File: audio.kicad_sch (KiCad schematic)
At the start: 5 parts, among them J3 Conn_01x02, U3 MAX98357A

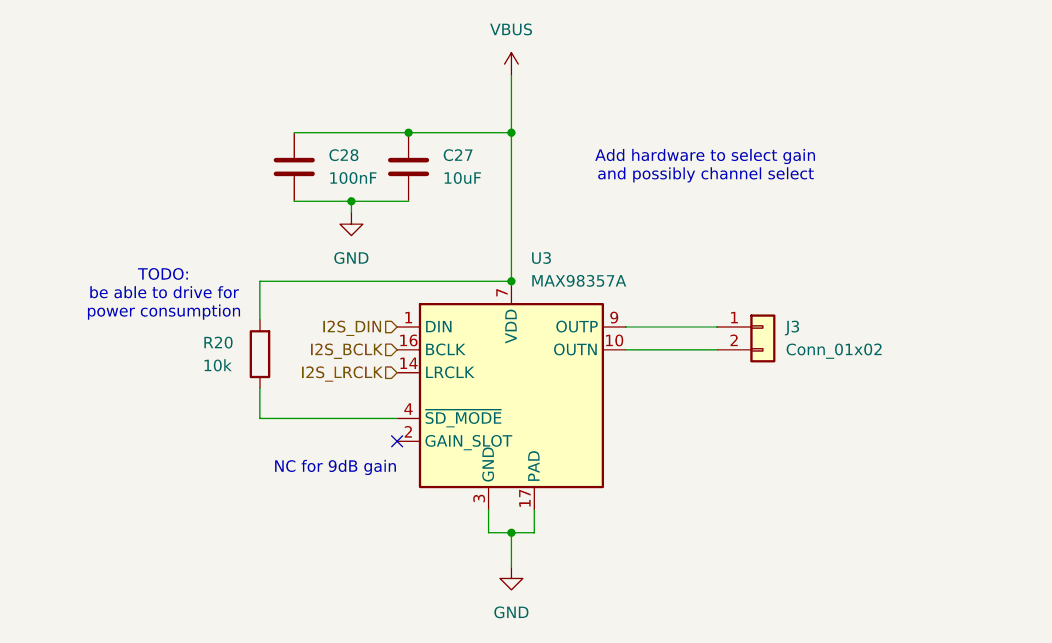
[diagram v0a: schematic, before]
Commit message: add amplifier mode selector, add drawing lcd
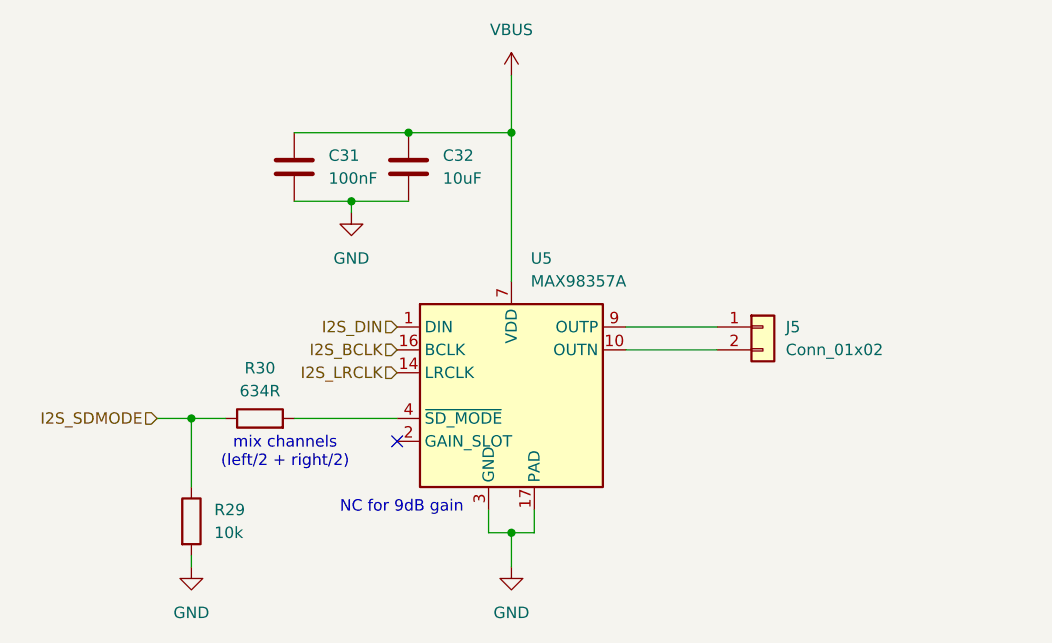
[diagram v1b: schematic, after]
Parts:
- removed R20: 10k, Resistor_SMD:R_0603_1608Metric, symbol Device:R
- added R29: 10k, symbol Device:R
- added R30: 634R, symbol Device:R
- renumbered C28 to C31, C27 to C32, J3 to J5, U3 to U5
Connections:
- net GND: now also R29.2
- net at U5.4 (~{SD_MODE}): now also R30.2
- new net I2S_SDMODE: R29.1, R30.1
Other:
- note added: "mix channels (left/2 + right/2)"
- note removed: "Add hardware to select gain and possibly channel select"
- note removed: "TODO: be able to drive for power consumption"

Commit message: add on/off switch
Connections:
- net VBUS renamed +5V

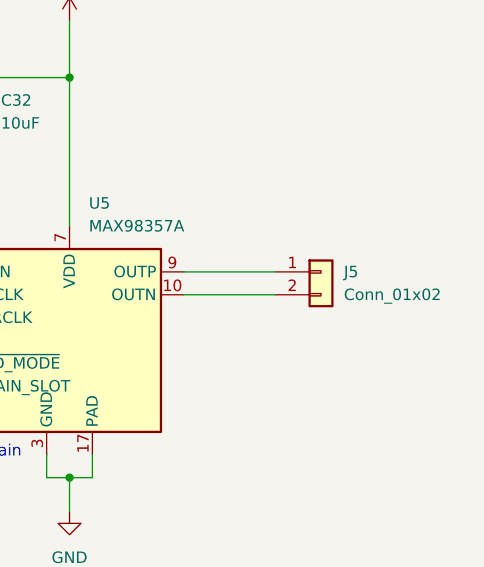
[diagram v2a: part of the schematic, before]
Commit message: add SD card
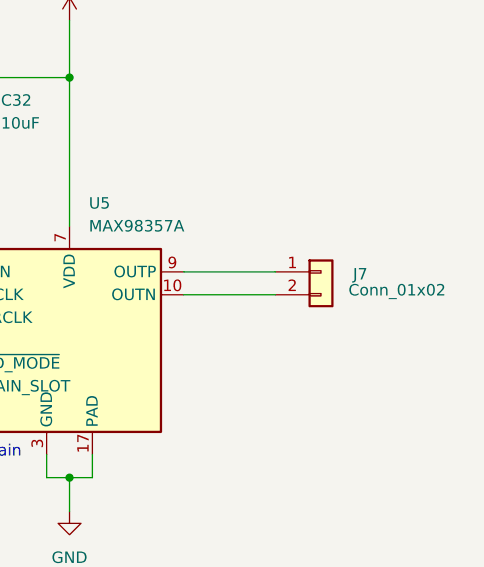
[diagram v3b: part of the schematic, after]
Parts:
- removed J5: Conn_01x02, symbol Connector_Generic:Conn_01x02
- added J7: Conn_01x02, Connector_JST:JST_PH_B2B-PH-K_1x02_P2.00mm_Vertical, symbol Connector_Generic:Conn_01x02
- C31: footprint (none) -> Capacitor_SMD:C_0603_1608Metric
- C32: footprint (none) -> Capacitor_SMD:C_0805_2012Metric
- R29, R30: footprint (none) -> Resistor_SMD:R_0603_1608Metric
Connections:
- net at U5.9 (OUTP): now also J7.1 (Pin_1)
- net at U5.10 (OUTN): now also J7.2 (Pin_2)
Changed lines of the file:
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@@
 			)
 		)
-		(property "Footprint" ""
+		(property "Footprint" "Resistor_SMD:R_0603_1608Metric"
 			(at 96.012 113.03 90)
 			(effects
@@
 	)
 	(symbol
-		(lib_id "Connector_Generic:Conn_01x02")
-		(at 161.29 91.44 0)
-		(unit 1)
-		(exclude_from_sim no)
-		(in_bom yes)
-		(on_board yes)
-		(dnp no)
-		(fields_autoplaced yes)
-		(property "Reference" "J5"
-			(at 163.83 91.4399 0)
-			(effects
-				(font
-					(size 1.27 1.27)
-				)
-				(justify left)
-			)
-		)
-		(property "Value" "Conn_01x02"
-			(at 163.83 93.9799 0)
-			(effects
-				(font
-					(size 1.27 1.27)
-				)
-				(justify left)
-			)
-		)
-		(property "Footprint" ""
-			(at 161.29 91.44 0)
-			(effects
-				(font
-					(size 1.27 1.27)
-				)
-				(hide yes)
-			)
-		)
-		(property "Datasheet" "~"
-			(at 161.29 91.44 0)
-			(effects
-				(font
-					(size 1.27 1.27)
-				)
-				(hide yes)
-			)
-		)
-		(property "Description" "Generic connector, single row, 01x02, script generated (kicad-library-utils/schlib/autogen/connector/)"
-			(at 161.29 91.44 0)
-			(effects
-				(font
-					(size 1.27 1.27)
-				)
-				(hide yes)
-			)
-		)
-		(pin "1"
-		)
-		(pin "2"
-		)
-		(instances
-			(project ""
-				(path "/f4643692-c319-40a7-82a2-3e775c0a417f/544a4a01-8cf8-45b3-bce5-8d02a4ea8581"
-					(reference "J5")
-					(unit 1)
-				)
-			)
-		)
-	)
-	(symbol
 		(lib_id "Device:R")
 		(at 105.41 101.6 90)
@@
 			)
 		)
-		(property "Footprint" ""
+		(property "Footprint" "Resistor_SMD:R_0603_1608Metric"
 			(at 105.41 103.378 90)
 			(effects
@@
 			)
 		)
-		(property "Footprint" ""
+		(property "Footprint" "Capacitor_SMD:C_0805_2012Metric"
 			(at 122.8852 77.47 0)
 			(effects
@@
 	)
 	(symbol
+		(lib_id "Connector_Generic:Conn_01x02")
+		(at 161.29 91.44 0)
+		(unit 1)
+		(exclude_from_sim no)
+		(in_bom yes)
+		(on_board yes)
+		(dnp no)
+		(property "Reference" "J7"
+			(at 164.846 91.694 0)
+			(effects
+				(font
+					(size 1.27 1.27)
+				)
+				(justify left)
+			)
+		)
+		(property "Value" "Conn_01x02"
+			(at 164.338 93.472 0)
+			(effects
+				(font
+					(size 1.27 1.27)
+				)
+				(justify left)
+			)
+		)
+		(property "Footprint" "Connector_JST:JST_PH_B2B-PH-K_1x02_P2.00mm_Vertical"
+			(at 161.29 91.44 0)
+			(effects
+				(font
+					(size 1.27 1.27)
+				)
+				(hide yes)
+			)
+		)
+		(property "Datasheet" "~"
+			(at 161.29 91.44 0)
+			(effects
+				(font
+					(size 1.27 1.27)
+				)
+				(hide yes)
+			)
+		)
+		(property "Description" "Generic connector, single row, 01x02, script generated (kicad-library-utils/schlib/autogen/connector/)"
+			(at 161.29 91.44 0)
+			(effects
+				(font
+					(size 1.27 1.27)
+				)
+				(hide yes)
+			)
+		)
+		(property "LCSC" "C131337"
+			(at 161.29 91.44 0)
+			(effects
+				(font
+					(size 1.27 1.27)
+				)
+				(hide yes)
+			)
+		)
+		(property "Manufacturer" "JST"
+			(at 161.29 91.44 0)
+			(effects
+				(font
+					(size 1.27 1.27)
+				)
+				(hide yes)
+			)
+		)
+		(property "Manufacturer Part Number" "B2B-PH-K-S(LF)(SN)"
+			(at 161.29 91.44 0)
+			(effects
+				(font
+					(size 1.27 1.27)
+				)
+				(hide yes)
+			)
+		)
+		(pin "2"
+		)
+		(pin "1"
+		)
+		(instances
+			(project "gameboy"
+				(path "/f4643692-c319-40a7-82a2-3e775c0a417f/544a4a01-8cf8-45b3-bce5-8d02a4ea8581"
+					(reference "J7")
+					(unit 1)
+				)
+			)
+		)
+	)
+	(symbol
 		(lib_id "power:+5V")
 		(at 133.35 63.5 0)
@@
 			)
 		)
-		(property "Footprint" ""
+		(property "Footprint" "Capacitor_SMD:C_0603_1608Metric"
 			(at 110.1852 77.47 0)
 			(effects

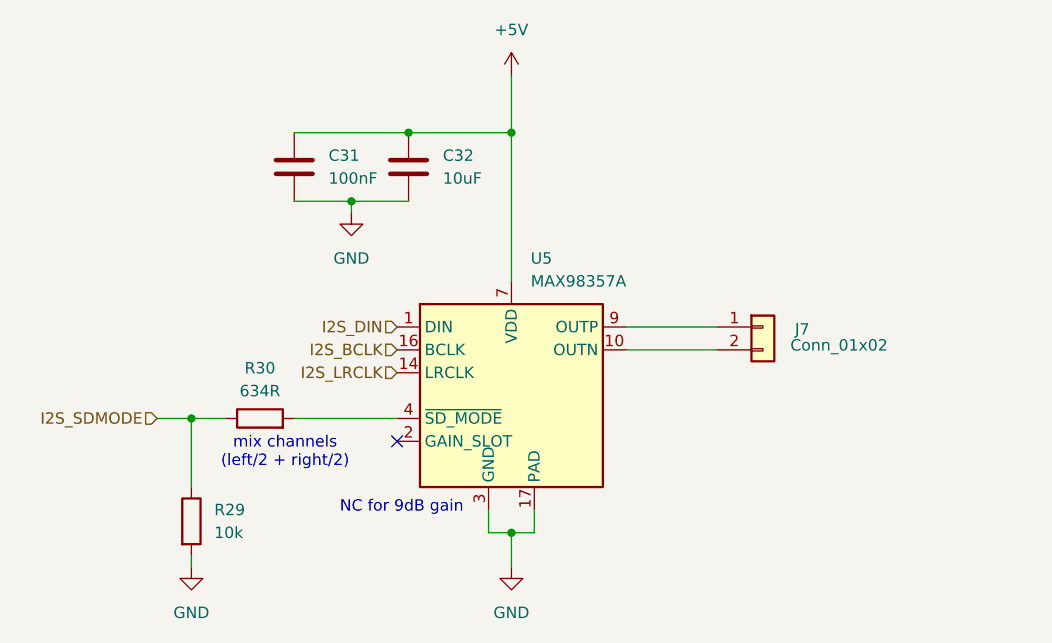
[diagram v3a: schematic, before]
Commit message: fix usb and add esd diodes, some other checks
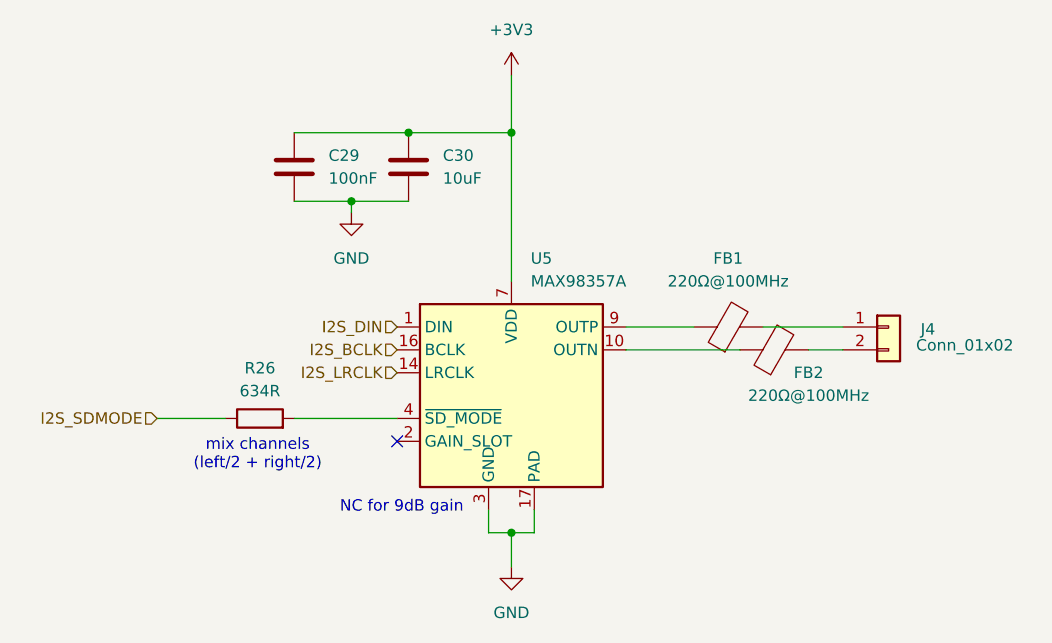
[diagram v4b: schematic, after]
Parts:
- removed R29: 10k, Resistor_SMD:R_0603_1608Metric, symbol Device:R
- added FB1, FB2: 220Ω@100MHz, Inductor_SMD:L_0603_1608Metric, symbol Device:FerriteBead
- renumbered C31 to C29, C32 to C30, J7 to J4, R30 to R26
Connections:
- net at U5.10 (OUTN): now also FB2.1; no longer J4.2 (Pin_2)
- net at U5.9 (OUTP): now also FB1.1; no longer J4.1 (Pin_1)
- net +5V renamed +3V3
- new net: FB1.2, J4.1 (Pin_1)
- new net: FB2.2, J4.2 (Pin_2)
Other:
- moved on the sheet: J4

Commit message: more routing
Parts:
- J4: footprint Connector_JST:JST_PH_B2B-PH-K_1x02_P2.00mm_Vertical -> Connector_JST:JST_PH_S2B-PH-SM4-TB_1x02-1MP_P2.00mm_Horizontal; LCSC C131337 -> C295747; Manufacturer Part Number B2B-PH-K-S(LF)(SN) -> S2B-PH-SM4-TB(LF)(SN)
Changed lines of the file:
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@@
+	)
+	(symbol
+		(lib_id "Connector_Generic:Conn_01x02")
+		(at 175.26 91.44 0)
+		(unit 1)
+		(exclude_from_sim no)
+		(in_bom yes)
+		(on_board yes)
+		(dnp no)
+		(property "Reference" "J4"
+			(at 178.816 91.694 0)
+			(effects
+				(font
+					(size 1.27 1.27)
+				)
+				(justify left)
+			)
+		)
+		(property "Value" "Conn_01x02"
+			(at 178.308 93.472 0)
+			(effects
+				(font
+					(size 1.27 1.27)
+				)
+				(justify left)
+			)
+		)
+		(property "Footprint" "Connector_JST:JST_PH_S2B-PH-SM4-TB_1x02-1MP_P2.00mm_Horizontal"
+			(at 175.26 91.44 0)
+			(effects
+				(font
+					(size 1.27 1.27)
+				)
+				(hide yes)
+			)
+		)
+		(property "Datasheet" "~"
+			(at 175.26 91.44 0)
+			(effects
+				(font
+					(size 1.27 1.27)
+				)
+				(hide yes)
+			)
+		)
+		(property "Description" "Generic connector, single row, 01x02, script generated (kicad-library-utils/schlib/autogen/connector/)"
+			(at 175.26 91.44 0)
+			(effects
+				(font
+					(size 1.27 1.27)
+				)
+				(hide yes)
+			)
+		)
+		(property "LCSC" "C295747"
+			(at 175.26 91.44 0)
+			(effects
+				(font
+					(size 1.27 1.27)
+				)
+				(hide yes)
+			)
+		)
+		(property "Manufacturer" "JST"
+			(at 175.26 91.44 0)
+			(effects
+				(font
+					(size 1.27 1.27)
+				)
+				(hide yes)
+			)
+		)
+		(property "Manufacturer Part Number" "S2B-PH-SM4-TB(LF)(SN)"
+			(at 175.26 91.44 0)
+			(effects
+				(font
+					(size 1.27 1.27)
+				)
+				(hide yes)
+			)
+		)
+		(pin "2"
+		)
+		(pin "1"
+		)
+		(instances
+			(project "gameboy"
+				(path "/f4643692-c319-40a7-82a2-3e775c0a417f/544a4a01-8cf8-45b3-bce5-8d02a4ea8581"
+					(reference "J4")
+					(unit 1)
+				)
+			)
+		)
 	)
 	(symbol
@@
 					(unit 1)
 				)
-			)
-		)
-	)
-	(symbol
-		(lib_id "Connector_Generic:Conn_01x02")
-		(at 175.26 91.44 0)
-		(unit 1)
-		(exclude_from_sim no)
-		(in_bom yes)
-		(on_board yes)
-		(dnp no)
-		(property "Reference" "J4"
-			(at 178.816 91.694 0)
-			(effects
-				(font
-					(size 1.27 1.27)
-				)
-				(justify left)
-			)
-		)
-		(property "Value" "Conn_01x02"
-			(at 178.308 93.472 0)
-			(effects
-				(font
-					(size 1.27 1.27)
-				)
-				(justify left)
-			)
-		)
-		(property "Footprint" "Connector_JST:JST_PH_B2B-PH-K_1x02_P2.00mm_Vertical"
-			(at 175.26 91.44 0)
-			(effects
-				(font
-					(size 1.27 1.27)
-				)
-				(hide yes)
-			)
-		)
-		(property "Datasheet" "~"
-			(at 175.26 91.44 0)
-			(effects
-				(font
-					(size 1.27 1.27)
-				)
-				(hide yes)
-			)
-		)
-		(property "Description" "Generic connector, single row, 01x02, script generated (kicad-library-utils/schlib/autogen/connector/)"
-			(at 175.26 91.44 0)
-			(effects
-				(font
-					(size 1.27 1.27)
-				)
-				(hide yes)
-			)
-		)
-		(property "LCSC" "C131337"
-			(at 175.26 91.44 0)
-			(effects
-				(font
-					(size 1.27 1.27)
-				)
-				(hide yes)
-			)
-		)
-		(property "Manufacturer" "JST"
-			(at 175.26 91.44 0)
-			(effects
-				(font
-					(size 1.27 1.27)
-				)
-				(hide yes)
-			)
-		)
-		(property "Manufacturer Part Number" "B2B-PH-K-S(LF)(SN)"
-			(at 175.26 91.44 0)
-			(effects
-				(font
-					(size 1.27 1.27)
-				)
-				(hide yes)
-			)
-		)
-		(pin "2"
-		)
-		(pin "1"
-		)
-		(instances
-			(project "gameboy"
-				(path "/f4643692-c319-40a7-82a2-3e775c0a417f/544a4a01-8cf8-45b3-bce5-8d02a4ea8581"
-					(reference "J4")
-					(unit 1)
-				)

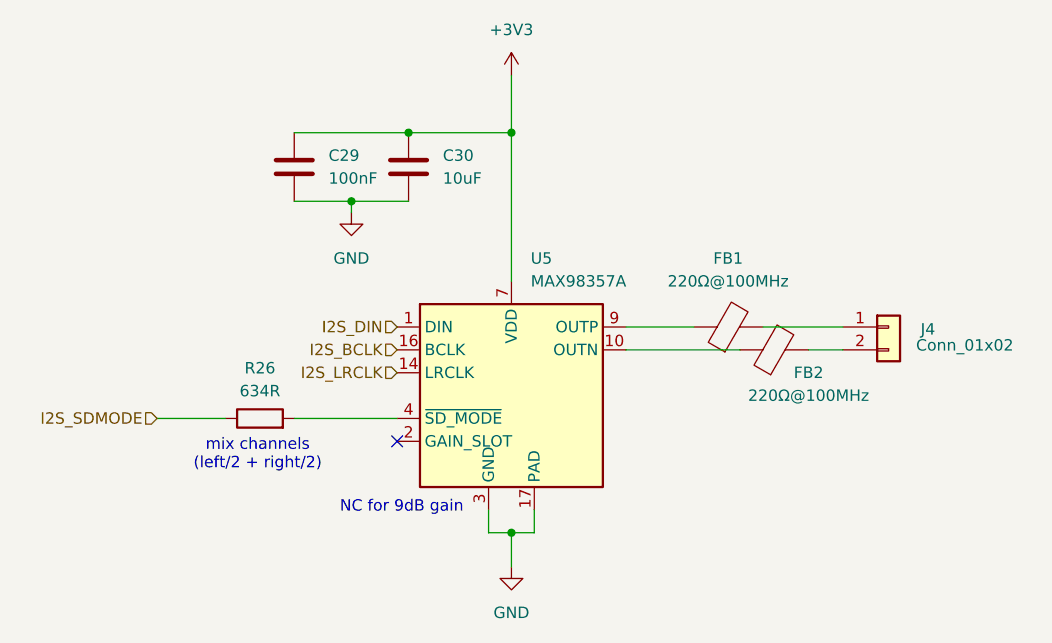
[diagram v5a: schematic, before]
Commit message: add silkscreen, optimize layout and replace sd card peripheral
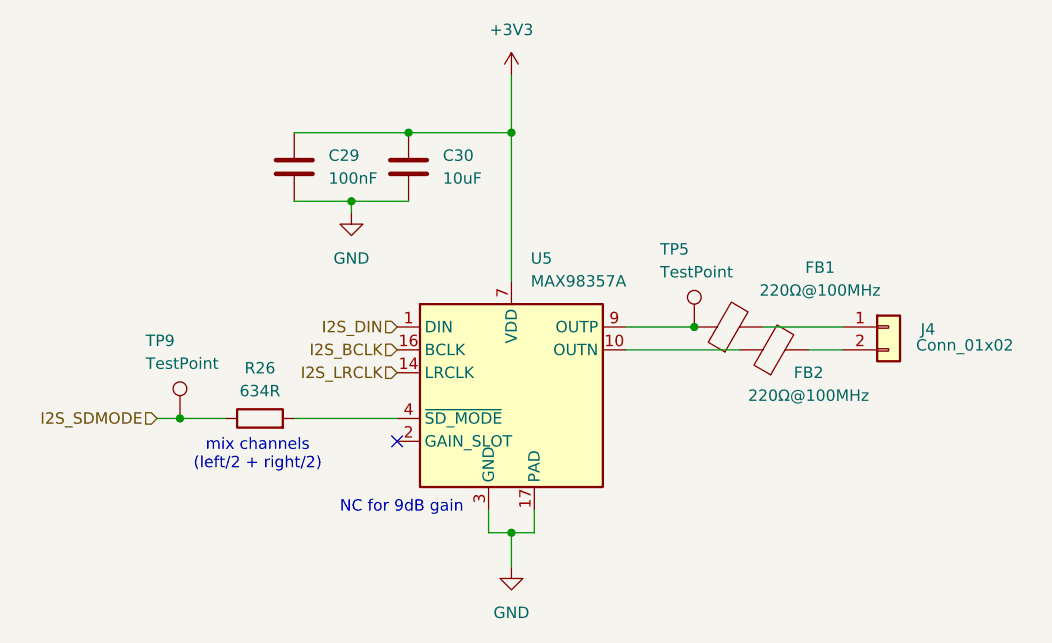
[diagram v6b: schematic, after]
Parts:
- added TP5, TP9: TestPoint, TestPoint:TestPoint_Pad_D1.0mm, symbol Connector:TestPoint
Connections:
- net I2S_SDMODE: now also TP9.1
- net at FB1.1, U5.9 (OUTP): now also TP5.1
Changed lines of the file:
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@@
+	)
+	(junction
+		(at 153.67 91.44)
+		(diameter 0)
+		(color 0 0 0 0)
 	)
 	(junction
@@
 	)
 	(junction
+		(at 96.52 101.6)
+		(diameter 0)
+		(color 0 0 0 0)
+	)
+	(junction
 		(at 121.92 69.85)
 		(diameter 0)
@@
 	(wire
 		(pts
-			(xy 93.98 101.6) (xy 101.6 101.6)
+			(xy 93.98 101.6) (xy 96.52 101.6)
 		)
 		(stroke
@@
 		(pts
 			(xy 161.29 91.44) (xy 170.18 91.44)
+		)
+		(stroke
+			(width 0)
+			(type default)
+		)
+	)
+	(wire
+		(pts
+			(xy 96.52 101.6) (xy 101.6 101.6)
 		)
 		(stroke
@@
 			)
 			(justify right)
+		)
+	)
+	(symbol
+		(lib_id "Connector:TestPoint")
+		(at 96.52 101.6 0)
+		(unit 1)
+		(exclude_from_sim no)
+		(in_bom yes)
+		(on_board yes)
+		(dnp no)
+		(property "Reference" "TP9"
+			(at 92.71 92.964 0)
+			(effects
+				(font
+					(size 1.27 1.27)
+				)
+				(justify left)
+			)
+		)
+		(property "Value" "TestPoint"
+			(at 92.71 95.504 0)
+			(effects
+				(font
+					(size 1.27 1.27)
+				)
+				(justify left)
+			)
+		)
+		(property "Footprint" "TestPoint:TestPoint_Pad_D1.0mm"
+			(at 101.6 101.6 0)
+			(effects
+				(font
+					(size 1.27 1.27)
+				)
+				(hide yes)
+			)
+		)
+		(property "Datasheet" "~"
+			(at 101.6 101.6 0)
+			(effects
+				(font
+					(size 1.27 1.27)
+				)
+				(hide yes)
+			)
+		)
+		(property "Description" "test point"
+			(at 96.52 101.6 0)
+			(effects
+				(font
+					(size 1.27 1.27)
+				)
+				(hide yes)
+			)
+		)
+		(property "LCSC" ""
+			(at 96.52 101.6 0)
+			(effects
+				(font
+					(size 1.27 1.27)
+				)
+				(hide yes)
+			)
+		)
+		(property "Manufacturer" ""
+			(at 96.52 101.6 0)
+			(effects
+				(font
+					(size 1.27 1.27)
+				)
+				(hide yes)
+			)
+		)
+		(property "Manufacturer Part Number" ""
+			(at 96.52 101.6 0)
+			(effects
+				(font
+					(size 1.27 1.27)
+				)
+				(hide yes)
+			)
+		)
+		(pin "1"
+		)
+		(instances
+			(project "gameboy"
+				(path "/f4643692-c319-40a7-82a2-3e775c0a417f/544a4a01-8cf8-45b3-bce5-8d02a4ea8581"
+					(reference "TP9")
+					(unit 1)
+				)
+			)
 		)
 	)
@@
 		(on_board yes)
 		(dnp no)
-		(fields_autoplaced yes)
 		(property "Reference" "FB1"
-			(at 157.4292 83.82 90)
+			(at 167.64 84.836 90)
 			(effects
 				(font
@@
 		)
 		(property "Value" "220Ω@100MHz"
-			(at 157.4292 86.36 90)
+			(at 167.64 87.376 90)
 			(effects
 				(font
@@
 					(unit 1)
 				)
+			)
+		)
+	)
+	(symbol
+		(lib_id "Connector:TestPoint")
+		(at 153.67 91.44 0)
+		(unit 1)
+		(exclude_from_sim no)
+		(in_bom yes)
+		(on_board yes)
+		(dnp no)
+		(property "Reference" "TP5"
+			(at 149.86 82.804 0)
+			(effects
+				(font
+					(size 1.27 1.27)
+				)
+				(justify left)
+			)
+		)
+		(property "Value" "TestPoint"
+			(at 149.86 85.344 0)
+			(effects
+				(font
+					(size 1.27 1.27)
+				)
+				(justify left)
+			)
+		)
+		(property "Footprint" "TestPoint:TestPoint_Pad_D1.0mm"
+			(at 158.75 91.44 0)
+			(effects
+				(font
+					(size 1.27 1.27)
+				)
+				(hide yes)
+			)
+		)
+		(property "Datasheet" "~"
+			(at 158.75 91.44 0)
+			(effects
+				(font
+					(size 1.27 1.27)
+				)
+				(hide yes)
+			)
+		)
+		(property "Description" "test point"
+			(at 153.67 91.44 0)
+			(effects
+				(font
+					(size 1.27 1.27)
+				)
+				(hide yes)
+			)
+		)
+		(property "LCSC" ""
+			(at 153.67 91.44 0)
+			(effects
+				(font
+					(size 1.27 1.27)
+				)
+				(hide yes)
+			)
+		)
+		(property "Manufacturer" ""
+			(at 153.67 91.44 0)
+			(effects
+				(font
+					(size 1.27 1.27)
+				)
+				(hide yes)
+			)
+		)
+		(property "Manufacturer Part Number" ""
+			(at 153.67 91.44 0)
+			(effects
+				(font
+					(size 1.27 1.27)
+				)
+				(hide yes)
+			)
+		)
+		(pin "1"
+		)
+		(instances
+			(project "gameboy"
+				(path "/f4643692-c319-40a7-82a2-3e775c0a417f/544a4a01-8cf8-45b3-bce5-8d02a4ea8581"
+					(reference "TP5")
+					(unit 1)
+				)
